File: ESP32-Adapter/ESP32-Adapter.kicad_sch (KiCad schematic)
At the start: 22 parts, among them J10 Barrel_Jack, J12 Conn_01x05, J13 Conn_01x05, J5 Conn_01x03, U1 ICM-42670-P_Click, U2 LM317DCYR, U3 Adafruit CANPAL, U4 ADAFRUIT INA219 BREAKOUT, U5 ESP32-S3-DevKitC

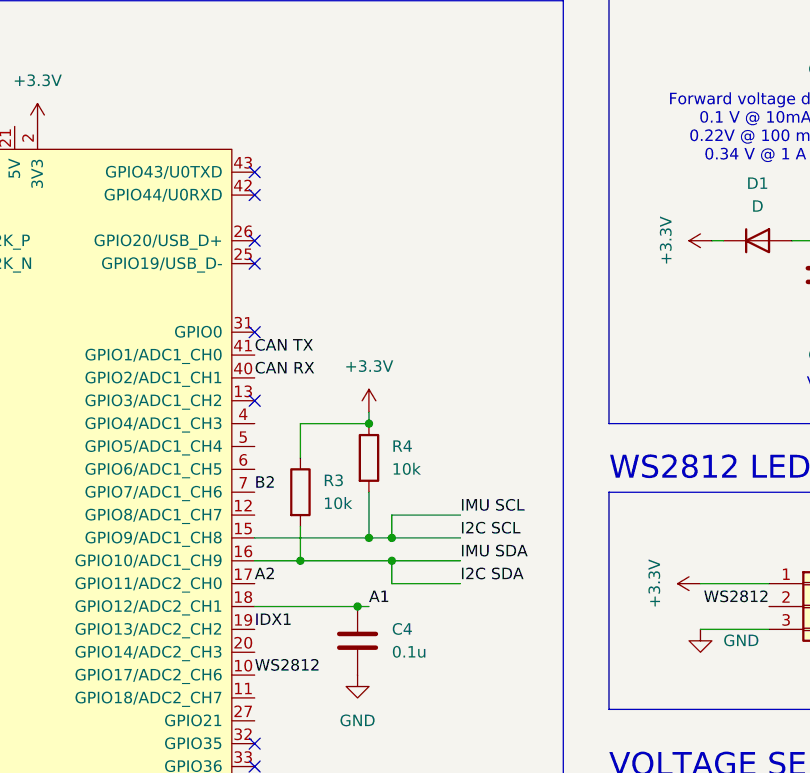
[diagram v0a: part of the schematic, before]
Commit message: add caps to A2 and B2
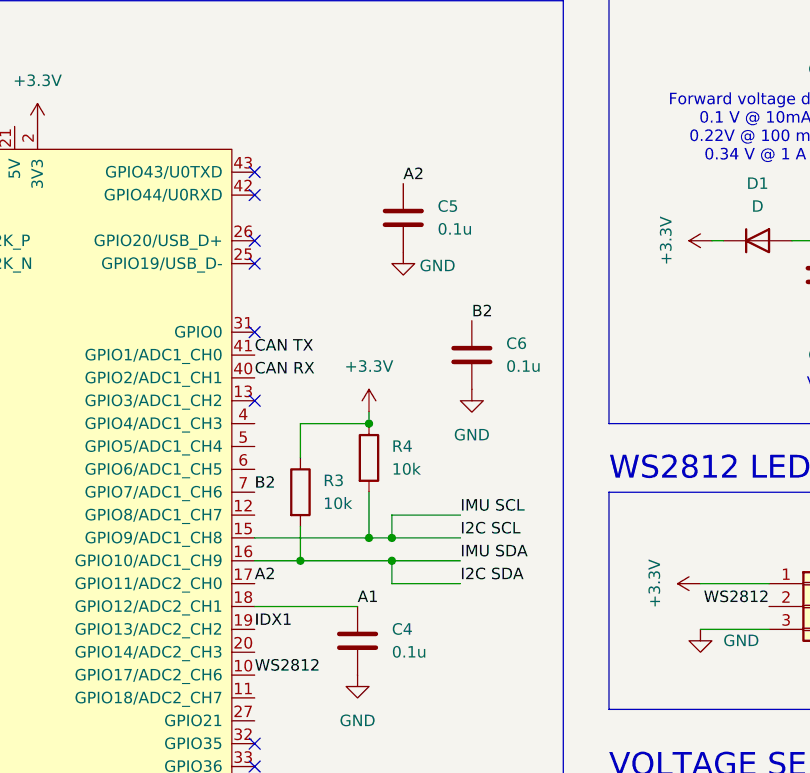
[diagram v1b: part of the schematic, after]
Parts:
- added C5, C6: 0.1u, Capacitor_SMD:C_0402_1005Metric, symbol Device:C
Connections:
- net A2: now also C5.1
- net B2: now also C6.1
- net GND: now also C5.2, C6.2

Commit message: added uart connections
Used gpio 17 & 18 for tx and rx
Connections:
- net +3.3V: no longer J5.1 (Pin_1)
- net UART_RX: now reaches U5.11 (GPIO18/ADC2_CH7)
- net UART_RX: now also J5.2 (Pin_2)
- net WS2812 renamed UART_TX
- net UART_TX: now also J5.1 (Pin_1); no longer J5.2 (Pin_2)
- no-connect marks 28 -> 29
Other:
- note added: "UART JST"
- note removed: "WS2812 LEDs"
- moved on the sheet: C5
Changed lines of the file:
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@@
 		)
 	)
-	(text "WS2812 LEDs"
+	(text "UART JST "
 		(exclude_from_sim no)
 		(at 251.46 167.64 0)
@@
 	)
 	(no_connect
+		(at 212.09 134.62)
+	)
+	(no_connect
 		(at 273.05 224.79)
 	)
@@
 	)
 	(no_connect
+		(at 212.09 137.16)
+	)
+	(no_connect
 		(at 212.09 200.66)
 	)
@@
 	)
 	(no_connect
-		(at 212.09 137.16)
-	)
-	(no_connect
 		(at 212.09 144.78)
 	)
@@
 	)
 	(no_connect
-		(at 212.09 134.62)
-	)
-	(no_connect
 		(at 273.05 222.25)
 	)
@@
 	)
 	(no_connect
+		(at 212.09 195.58)
+	)
+	(no_connect
 		(at 110.49 163.83)
 	)
@@
 	(wire
 		(pts
+			(xy 261.62 182.88) (xy 269.24 182.88)
+		)
+		(stroke
+			(width 0)
+			(type default)
+		)
+	)
+	(wire
+		(pts
 			(xy 281.94 142.24) (xy 283.21 142.24)
 		)
@@
 	)
 	(label "A2"
-		(at 228.6 135.89 0)
+		(at 236.22 135.89 0)
 		(effects
 			(font
@@
 		)
 	)
+	(label "UART_TX"
+		(at 212.09 190.5 0)
+		(effects
+			(font
+				(size 1.27 1.27)
+			)
+			(justify left bottom)
+		)
+	)
+	(label "UART_RX"
+		(at 212.09 193.04 0)
+		(effects
+			(font
+				(size 1.27 1.27)
+			)
+			(justify left bottom)
+		)
+	)
 	(label "IDX1"
 		(at 212.09 185.42 0)
@@
 		)
 	)
+	(label "UART_RX"
+		(at 261.62 182.88 180)
+		(effects
+			(font
+				(size 1.27 1.27)
+			)
+			(justify right bottom)
+		)
+	)
 	(label "B2"
 		(at 212.09 170.18 0)
@@
 		)
 	)
-	(label "WS2812"
-		(at 212.09 190.5 0)
-		(effects
-			(font
-				(size 1.27 1.27)
-			)
-			(justify left bottom)
-		)
-	)
 	(label "I2C SCL"
 		(at 234.95 175.26 0)
@@
 		)
 	)
-	(label "WS2812"
-		(at 269.24 182.88 180)
-		(effects
-			(font
-				(size 1.27 1.27)
-			)
-			(justify right bottom)
-		)
-	)
 	(label "IDX2"
 		(at 111.76 135.89 0)
@@
 		)
 	)
+	(label "UART_TX"
+		(at 261.62 180.34 180)
+		(effects
+			(font
+				(size 1.27 1.27)
+			)
+			(justify right bottom)
+		)
+	)
 	(label "IDX1"
 		(at 111.76 120.65 0)
@@
 	)
 	(symbol
-		(lib_id "power:+3.3V")
-		(at 261.62 180.34 90)
-		(mirror x)
-		(unit 1)
-		(exclude_from_sim no)
-		(in_bom yes)
-		(on_board yes)
-		(dnp no)
-		(property "Reference" "#PWR012"
-			(at 265.43 180.34 0)
-			(effects
-				(font
-					(size 1.27 1.27)
-				)
-				(hide yes)
-			)
-		)
-		(property "Value" "+3.3V"
-			(at 256.54 180.34 0)
-			(effects
-				(font
-					(size 1.27 1.27)
-				)
-			)
-		)
-		(property "Footprint" ""
-			(at 261.62 180.34 0)
-			(effects
-				(font
-					(size 1.27 1.27)
-				)
-				(hide yes)
-			)
-		)
-		(property "Datasheet" ""
-			(at 261.62 180.34 0)
-			(effects
-				(font
-					(size 1.27 1.27)
-				)
-				(hide yes)
-			)
-		)
-		(property "Description" "Power symbol creates a global label with name \"+3.3V\""
-			(at 261.62 180.34 0)
-			(effects
-				(font
-					(size 1.27 1.27)
-				)
-				(hide yes)
-			)
-		)
-		(pin "1"
-		)
-		(instances
-			(project "ESP32-Adapter"
-				(path "/69a61e70-b602-4412-b60e-1eedbaac8100"
-					(reference "#PWR012")
-					(unit 1)
-				)
-			)
-		)
-	)
-	(symbol
 		(lib_id "Mechanical:MountingHole")
 		(at 175.26 250.19 0)
@@
 	(symbol
 		(lib_id "power:GND")
-		(at 228.6 143.51 0)
+		(at 236.22 143.51 0)
 		(mirror y)
 		(unit 1)
@@
 		(dnp no)
 		(property "Reference" "#PWR022"
-			(at 228.6 149.86 0)
+			(at 236.22 149.86 0)
 			(effects
 				(font
@@
 		)
 		(property "Value" "GND"
-			(at 232.41 145.034 0)
+			(at 240.03 145.034 0)
 			(effects
 				(font
@@
 		)
 		(property "Footprint" ""
-			(at 228.6 143.51 0)
+			(at 236.22 143.51 0)
 			(effects
 				(font
@@
 		)
 		(property "Datasheet" ""
-			(at 228.6 143.51 0)
+			(at 236.22 143.51 0)
 			(effects
 				(font
@@
 		)
 		(property "Description" "Power symbol creates a global label with name \"GND\" , ground"
-			(at 228.6 143.51 0)
+			(at 236.22 143.51 0)
 			(effects
 				(font
@@
 	(symbol
 		(lib_id "Device:C")
-		(at 228.6 139.7 0)
+		(at 236.22 139.7 0)
 		(unit 1)
 		(exclude_from_sim no)
@@
 		(dnp no)
 		(property "Reference" "C5"
-			(at 232.41 138.4299 0)
+			(at 240.03 138.4299 0)
 			(effects
 				(font
@@
 		)
 		(property "Value" "0.1u"
-			(at 232.41 140.9699 0)
+			(at 240.03 140.9699 0)
 			(effects
 				(font
@@
 		)
 		(property "Footprint" "Capacitor_SMD:C_0402_1005Metric"
-			(at 229.5652 143.51 0)
+			(at 237.1852 143.51 0)
 			(effects
 				(font
@@
 		)
 		(property "Datasheet" "~"
-			(at 228.6 139.7 0)
+			(at 236.22 139.7 0)
 			(effects
 				(font
@@
 		)
 		(property "Description" "Unpolarized capacitor"
-			(at 228.6 139.7 0)
+			(at 236.22 139.7 0)
 			(effects
 				(font

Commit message: made j5 vertical as per jarad e
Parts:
- J5: footprint Connector_JST:JST_XH_S3B-XH-A-1_1x03_P2.50mm_Horizontal -> Connector_JST:JST_XH_B3B-XH-A_1x03_P2.50mm_Vertical
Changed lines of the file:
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@@
 			)
 		)
-		(property "Footprint" "Connector_JST:JST_XH_S3B-XH-A-1_1x03_P2.50mm_Horizontal"
+		(property "Footprint" "Connector_JST:JST_XH_B3B-XH-A_1x03_P2.50mm_Vertical"
 			(at 274.32 182.88 0)
 			(effects

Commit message: Change JST-XH connectors to vertical
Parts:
- J12, J13: footprint Connector_JST:JST_XH_S5B-XH-A-1_1x05_P2.50mm_Horizontal -> Connector_JST:JST_XH_B5B-XH-A_1x05_P2.50mm_Vertical
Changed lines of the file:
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@@
 			)
 		)
-		(property "Footprint" "Connector_JST:JST_XH_S5B-XH-A-1_1x05_P2.50mm_Horizontal"
+		(property "Footprint" "Connector_JST:JST_XH_B5B-XH-A_1x05_P2.50mm_Vertical"
 			(at 106.68 138.43 0)
 			(effects
@@
 			)
 		)
-		(property "Footprint" "Connector_JST:JST_XH_S5B-XH-A-1_1x05_P2.50mm_Horizontal"
+		(property "Footprint" "Connector_JST:JST_XH_B5B-XH-A_1x05_P2.50mm_Vertical"
 			(at 106.68 123.19 0)
 			(effects
